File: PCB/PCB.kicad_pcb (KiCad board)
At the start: 4 copper layers, 75 x 75 mm, 113 parts, among them J1 Conn_01x06_Female, J2 5054332681, U1 Hx711, U10 Hx711, U11 Hx711, U12 Hx711, U13 74HC165, U15 LT3042xMSE, U16 74HC165, U2 Hx711, U3 Hx711, U4 Hx711, U5 Hx711, U6 Hx711, U7 Hx711, U8 Hx711, U9 Hx711

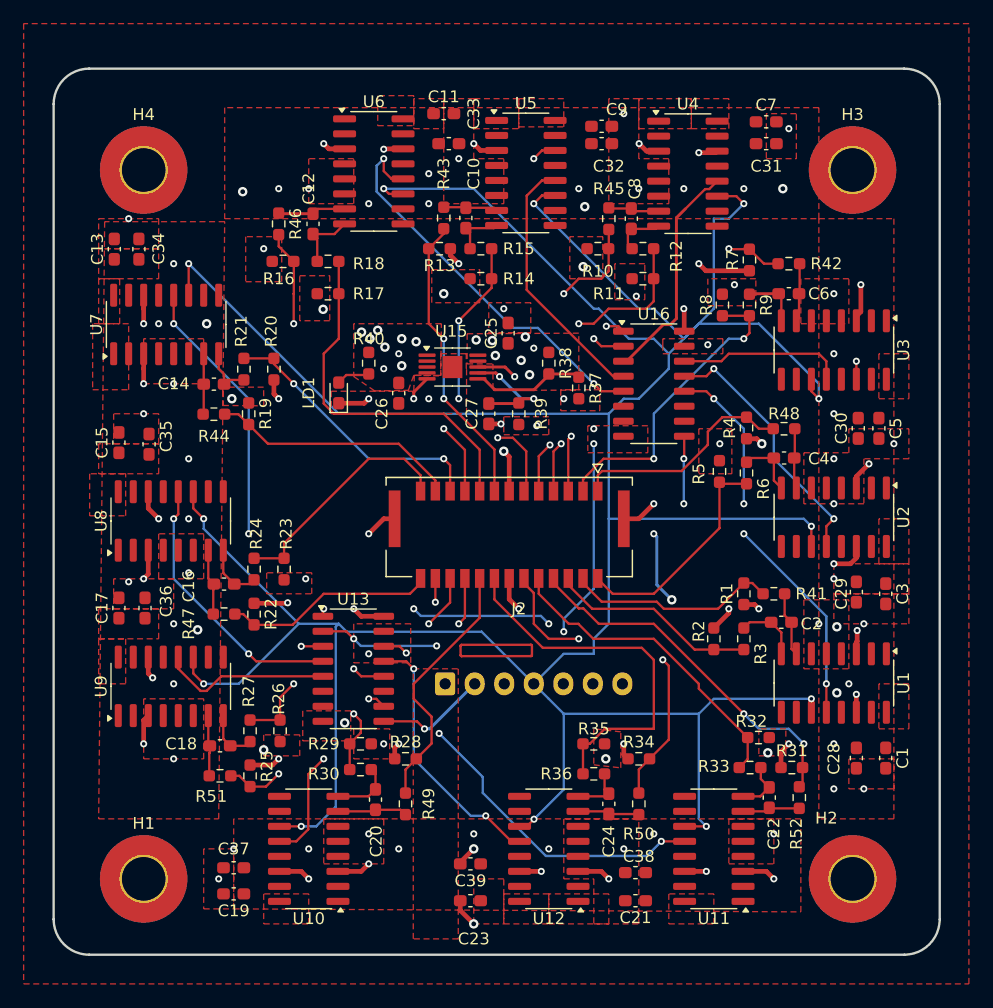
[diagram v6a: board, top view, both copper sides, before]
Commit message: Board updated for linear regulator and fills
Fills around each of the hx711 capacitor assemblies were changed to solid fills and the layout around the linear regulator was optimized to better fit with the data sheet.
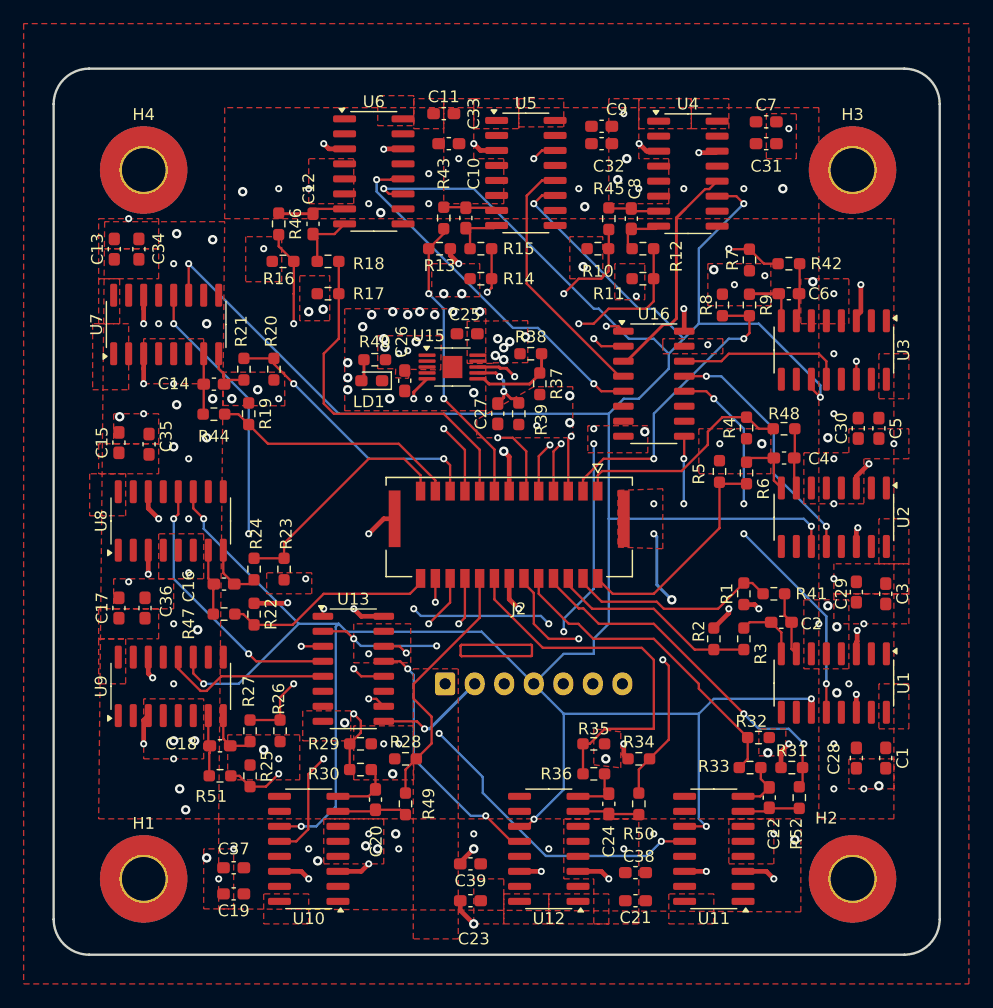
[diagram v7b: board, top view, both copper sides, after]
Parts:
- moved C25 3.47 mm to (243.3, 106.3), turned to 180 degrees
- moved R37 3.32 mm to (249.4, 110.5)
- moved LD1 2.98 mm to (235.2, 110.2), turned to 180 degrees
- moved R38 1.72 mm to (248.7, 108.0), turned to 0 degrees
- moved C26 1.17 mm to (238.0, 110.2)
- moved C27 0.76 mm to (245.9, 113.0)
- moved R40 0.59 mm to (235.5, 108.5), turned to 180 degrees
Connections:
- U15 pad 4: +5V -> unconnected-(U15-PG-Pad4)
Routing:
- net GND: track 68.4 -> 48.4 mm, vias 74 -> 102
- net Net-(U15-SET): track 9.96 -> 6.90 mm
- net HX_CLK: track 305.4 -> 302.5 mm
- net /DOUT10: track 33.9 -> 31.2 mm
- net Net-(U15-PGFB): track 9.55 -> 7.34 mm
- net /DOUT12: track 22.3 -> 21.2 mm
- net Net-(LD1-A): track 2.81 -> 2.07 mm
- net /H9P: track 26.4 -> 25.7 mm
- net 4.5V: track 36.5 -> 35.9 mm, vias 21 -> 20
- net /DOUT5: track 37.0 -> 36.5 mm
- net +5V: track 4.79 -> 4.72 mm, vias 43 -> 52
- net /H2N: vias 3 -> 2
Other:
- board text added: "+3.3V"
- board text added: "+5V"
- board text added: "DATA"
- board text added: "GND"
- board text added: "HX_CLK"
- board text added: "LOAD"
- board text added: "S_CLK"

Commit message: Added test points and changed labels
Added test points for nearly every single cable. Labels on individual sections changed to better reflect the actual board.
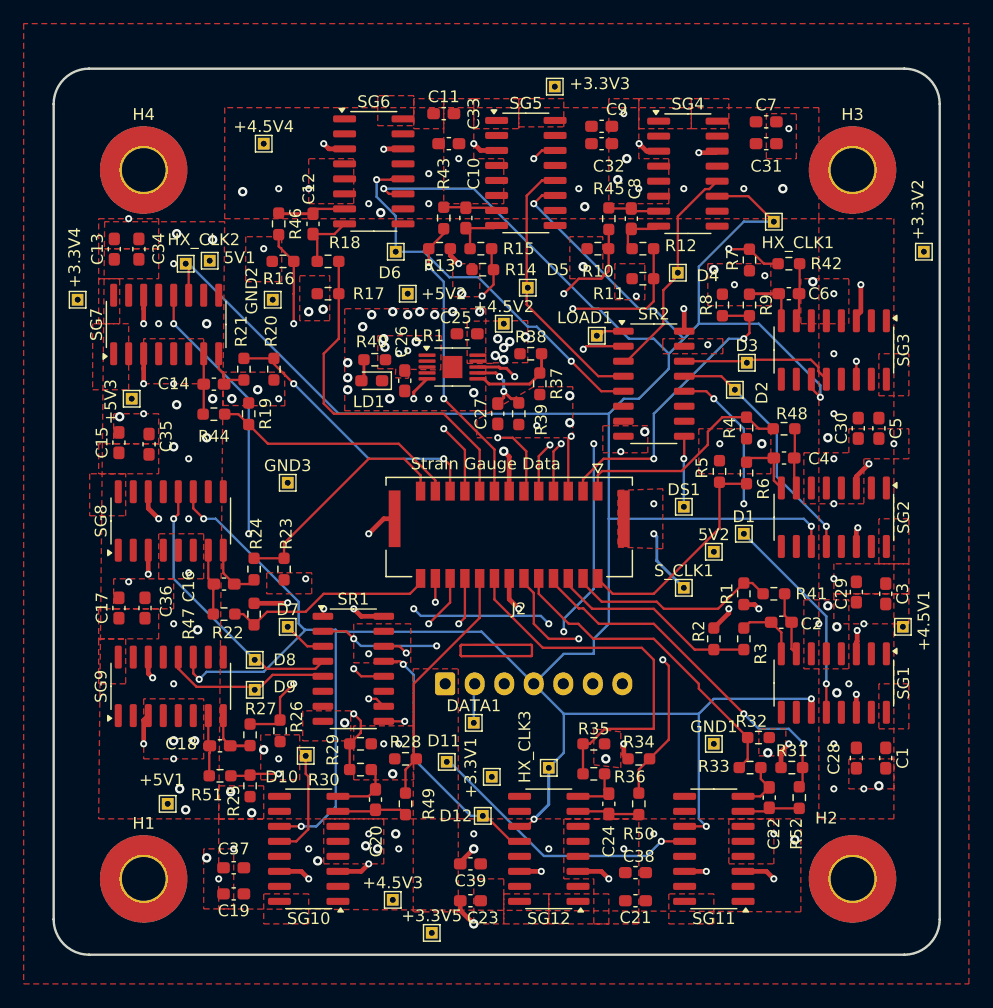
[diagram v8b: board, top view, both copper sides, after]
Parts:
- added +3.3V1: 3.3V, TestPoint:TestPoint_THTPad_1.0x1.0mm_Drill0.5mm, F.Cu at (245.4, 143.8)
- added +3.3V2: 3.3V, TestPoint:TestPoint_THTPad_1.0x1.0mm_Drill0.5mm, F.Cu at (281.9, 99.3)
- added +3.3V3: 3.3V, TestPoint:TestPoint_THTPad_1.0x1.0mm_Drill0.5mm, F.Cu at (250.7, 85.3)
- added +3.3V4: 3.3V, TestPoint:TestPoint_THTPad_1.0x1.0mm_Drill0.5mm, F.Cu at (210.3, 103.4)
- added +3.3V5: 3.3V, TestPoint:TestPoint_THTPad_1.0x1.0mm_Drill0.5mm, F.Cu at (240.3, 157.0)
- added +4.5V1: 4.5V, TestPoint:TestPoint_THTPad_1.0x1.0mm_Drill0.5mm, F.Cu at (280.2, 131.1)
- added +4.5V2: 4.5V, TestPoint:TestPoint_THTPad_1.0x1.0mm_Drill0.5mm, F.Cu at (246.4, 105.4)
- added +4.5V3: 4.5V, TestPoint:TestPoint_THTPad_1.0x1.0mm_Drill0.5mm, F.Cu at (237.0, 154.2)
- added +4.5V4: 4.5V, TestPoint:TestPoint_THTPad_1.0x1.0mm_Drill0.5mm, F.Cu at (226.1, 90.2)
- added +5V1: 5V, TestPoint:TestPoint_THTPad_1.0x1.0mm_Drill0.5mm, F.Cu at (217.9, 146.1)
- added +5V2: 5V, TestPoint:TestPoint_THTPad_1.0x1.0mm_Drill0.5mm, F.Cu at (238.3, 102.9)
- added +5V3: 5V, TestPoint:TestPoint_THTPad_1.0x1.0mm_Drill0.5mm, F.Cu at (214.9, 111.8)
- added 5V1: 5V, TestPoint:TestPoint_THTPad_1.0x1.0mm_Drill0.5mm, F.Cu at (221.5, 100.1)
- added 5V2: 5V, TestPoint:TestPoint_THTPad_1.0x1.0mm_Drill0.5mm, F.Cu at (264.2, 124.7)
- added D1: SG1, TestPoint:TestPoint_THTPad_1.0x1.0mm_Drill0.5mm, F.Cu at (266.7, 123.2)
- added D10: SG10, TestPoint:TestPoint_THTPad_1.0x1.0mm_Drill0.5mm, F.Cu at (229.6, 142.0)
- added D11: SG11, TestPoint:TestPoint_THTPad_1.0x1.0mm_Drill0.5mm, F.Cu at (241.6, 142.5)
- added D12: SG12, TestPoint:TestPoint_THTPad_1.0x1.0mm_Drill0.5mm, F.Cu at (244.6, 147.1)
- added D2: SG2, TestPoint:TestPoint_THTPad_1.0x1.0mm_Drill0.5mm, F.Cu at (265.9, 111.0)
- added D3: SGD3, TestPoint:TestPoint_THTPad_1.0x1.0mm_Drill0.5mm, F.Cu at (267.0, 108.7)
- added D4: SG4, TestPoint:TestPoint_THTPad_1.0x1.0mm_Drill0.5mm, F.Cu at (261.1, 101.1)
- added D5: SG5, TestPoint:TestPoint_THTPad_1.0x1.0mm_Drill0.5mm, F.Cu at (248.4, 102.4)
- added D6: SG6, TestPoint:TestPoint_THTPad_1.0x1.0mm_Drill0.5mm, F.Cu at (237.2, 99.3)
- added D7: SG7, TestPoint:TestPoint_THTPad_1.0x1.0mm_Drill0.5mm, F.Cu at (228.1, 131.1)
- added D8: SG8, TestPoint:TestPoint_THTPad_1.0x1.0mm_Drill0.5mm, F.Cu at (225.3, 133.9)
- added D9: SG9, TestPoint:TestPoint_THTPad_1.0x1.0mm_Drill0.5mm, F.Cu at (225.3, 136.4)
- added DATA1: DATA, TestPoint:TestPoint_THTPad_1.0x1.0mm_Drill0.5mm, F.Cu at (243.8, 139.2)
- added DS1: DS, TestPoint:TestPoint_THTPad_1.0x1.0mm_Drill0.5mm, F.Cu at (261.6, 120.9)
- added GND1: GND, TestPoint:TestPoint_THTPad_1.0x1.0mm_Drill0.5mm, F.Cu at (264.2, 141.0)
- added GND2: GND, TestPoint:TestPoint_THTPad_1.0x1.0mm_Drill0.5mm, F.Cu at (226.8, 103.4)
- added GND3: GND, TestPoint:TestPoint_THTPad_1.0x1.0mm_Drill0.5mm, F.Cu at (228.1, 118.9)
- added HX_CLK1: HX_CLK, TestPoint:TestPoint_THTPad_1.0x1.0mm_Drill0.5mm, F.Cu at (269.2, 96.8)
- added HX_CLK2: HX_CLK, TestPoint:TestPoint_THTPad_1.0x1.0mm_Drill0.5mm, F.Cu at (219.5, 100.3)
- added HX_CLK3: HX_CLK, TestPoint:TestPoint_THTPad_1.0x1.0mm_Drill0.5mm, F.Cu at (250.2, 143.0)
- added LOAD1: LOAD, TestPoint:TestPoint_THTPad_1.0x1.0mm_Drill0.5mm, F.Cu at (254.3, 106.4)
- added S_CLK1: S_CLK, TestPoint:TestPoint_THTPad_1.0x1.0mm_Drill0.5mm, F.Cu at (261.6, 127.8)
- moved R25 0.85 mm to (224.9, 144.5), turned to 90 degrees
- moved R14 0.78 mm to (244.6, 100.8)
- moved R27 0.34 mm to (224.9, 140.2)
- renumbered U15 to LR1, U1 to SG1, U10 to SG10, U11 to SG11, U12 to SG12, U2 to SG2, U3 to SG3, U4 to SG4, U5 to SG5, U6 to SG6, U7 to SG7, U8 to SG8, U9 to SG9, U13 to SR1, U16 to SR2
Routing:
- net HX_CLK: track 302.5 -> 306.8 mm, vias 12 -> 10
- net /DOUT10: track 31.2 -> 33.2 mm
- net /DATA: track 9.54 -> 10.9 mm
- net /H13P: track 22.0 -> 20.9 mm
- net /H9N: track 26.6 -> 27.7 mm
- net /DOUT2: track 21.8 -> 22.9 mm
- net /DOUT11: track 23.1 -> 23.8 mm, vias 2 -> 1
- net /H4P: track 28.2 -> 27.4 mm
- net /DOUT9: track 19.2 -> 18.6 mm
- net /DOUT1: track 14.1 -> 13.5 mm
- net /S_CLK: track 64.2 -> 64.5 mm, vias 5 -> 4
- net /DOUT13: track 20.8 -> 21.0 mm, vias 2 -> 1
- net /DOUT5: track 36.5 -> 36.7 mm, vias 3 -> 2
- net /DOUT3: track 36.0 -> 35.9 mm, vias 3 -> 2
- net /LOAD: track 55.3 -> 55.4 mm, vias 4 -> 3
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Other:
- board text added: "Flight Computer"
- board text added: "Strain Gauge Data"
